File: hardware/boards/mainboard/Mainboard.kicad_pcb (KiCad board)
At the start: 2 copper layers, 114.3 x 101.6 mm, 118 parts, among them IC1 LM340?-MP, J1 MOLEX_52892-3033MOLEX_52892-3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, J2 JST---S4B-PH-SM4-TB(LF)(SN)_J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, U1 CS42448, U2 PCA9536

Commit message: mainboard v1.7
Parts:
- removed J1: MOLEX_52892-3033MOLEX_52892-3033_0_0, Mainboard:MOLEX_52892-3033_0
- removed J2: JST---S4B-PH-SM4-TB(LF)(SN)_JST_S4B-PH-SM4-TB_LF_SNJST_S4B-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, knobs:JST---S4B-PH-SM4-TB(LF)(SN)_JST_S4B-PH-SM4-TB_LF_SN_0
- added U3: Breakoutboard, topbreakout:Breakoutboard, B.Cu at (17.8, 71.1)
- U$1: value TEENSY_4.0_WITH_SMD_HEADER_PINS -> TEENSY_4.0_WITH_SMD_HEADER_PINS_2; footprint Mainboard:TEENSY_4.0_WITH_SMD_HEADER_PINS -> Mainboard:TEENSY_4.0_WITH_SMD_HEADER_PINS_2
- moved JUSB_B1 76.9 mm to (26.0, 68.6)
- moved R1 14.4 mm to (45.7, 22.2)
- moved C54 8.64 mm to (24.8, 59.1)
- moved C53 8.64 mm to (24.8, 55.9)
- moved R31 8.64 mm to (24.9, 53.0)
- moved C51 8.13 mm to (31.8, 62.2)
- moved C49 7.18 mm to (24.8, 38.7)
- moved C50 7.18 mm to (24.8, 41.3)
- moved R27 7.18 mm to (24.9, 35.8)
- moved C47 7.17 mm to (31.7, 43.8)
- moved R33 6.99 mm to (64.1, 67.9)
- moved C52 6.75 mm to (31.8, 52.7)
- moved R29 6.75 mm to (31.8, 55.6)
- moved R30 6.75 mm to (31.8, 58.4)
- moved C43 6.35 mm to (31.8, 27.9)
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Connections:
- net /codec/LEFT renamed /codec/Audio-out/LEFT
- net /codec/LEFT_1 renamed /codec/sheet5D8B3355/LEFT
- net /codec/LEFT_2 renamed /codec/sheet5D8BB035/LEFT
- net /codec/LEFT_3 renamed /codec/sheet5D7A5ED6/LEFT
- net /codec/LEFT_OUT renamed /codec/Audio-in/LEFT_OUT
- net /codec/LEFT_OUT_1 renamed /codec/sheet5D7EAAD2/LEFT_OUT
- net /codec/LEFT_OUT_2 renamed /codec/sheet5D7E3893/LEFT_OUT
- net /codec/RIGHT renamed /codec/Audio-out/RIGHT
- net /codec/RIGHT_1 renamed /codec/sheet5D8BB035/RIGHT
- net /codec/RIGHT_2 renamed /codec/sheet5D8B3355/RIGHT
- net /codec/RIGHT_3 renamed /codec/sheet5D7A5ED6/RIGHT
- net /codec/RIGHT_OUT renamed /codec/sheet5D7E3893/RIGHT_OUT
- net /codec/RIGHT_OUT_1 renamed /codec/Audio-in/RIGHT_OUT
- net /codec/RIGHT_OUT_2 renamed /codec/sheet5D7EAAD2/RIGHT_OUT
- U1 pad 24: +3V3 -> 3V3
- U1 pad 4: +3V3 -> 3V3
- U1 pad 6: +3V3 -> 3V3
- U1 pad 8: +3V3 -> 3V3
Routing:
- net VIN: track 167.0 -> 0.00 mm, vias 1 -> 0
- net +3V3: track 165.0 -> 0.00 mm, vias 2 -> 0
- net SDA: track 148.5 -> 0.00 mm, vias 2 -> 0
- net SCL: track 143.3 -> 0.00 mm, vias 2 -> 0
- net /codec/AVIN: track 96.7 -> 0.00 mm
- net AVSS: track 94.2 -> 0.00 mm, vias 1 -> 0
- net AVDD: track 93.3 -> 0.00 mm, vias 1 -> 0
- net BCLK: track 92.2 -> 0.00 mm, vias 2 -> 0
- net LRCLK: track 87.0 -> 0.00 mm, vias 3 -> 0
- net MCLK: track 83.8 -> 0.00 mm, vias 2 -> 0
- net GND: track 69.6 -> 0.00 mm, vias 89 -> 0
- net DAC_DATA: track 65.3 -> 0.00 mm, vias 1 -> 0
- net ADC_DATA: track 64.1 -> 0.00 mm, vias 1 -> 0
- net /codec/sheet5D8BB035/RIGHT: track 53.5 -> 0.00 mm
- net GATE_1: track 49.1 -> 0.00 mm, vias 1 -> 0
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- removed copper zone on B.Cu, net /codec/AGND
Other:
- board size 114.3 x 101.6 mm -> 118.1 x 101.6 mm

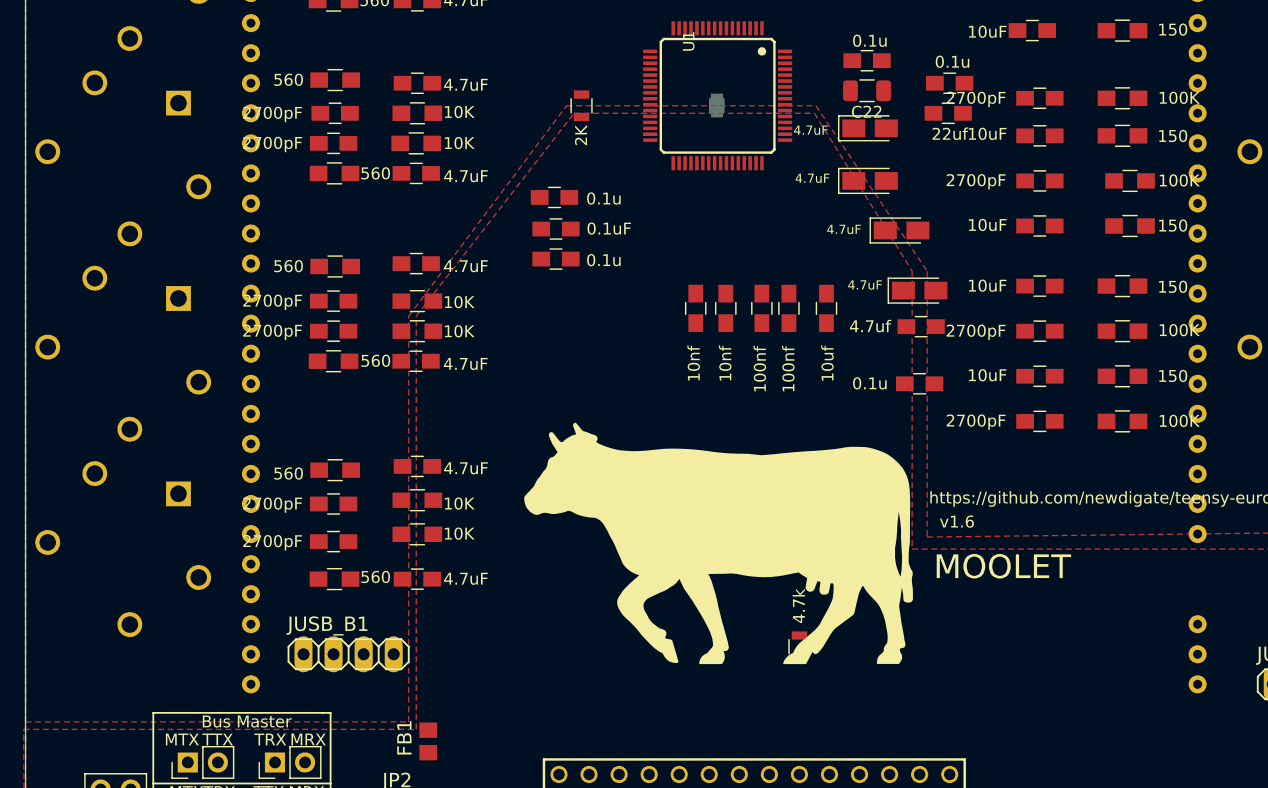
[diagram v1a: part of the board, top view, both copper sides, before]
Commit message: mainboard v1.7 minor changes
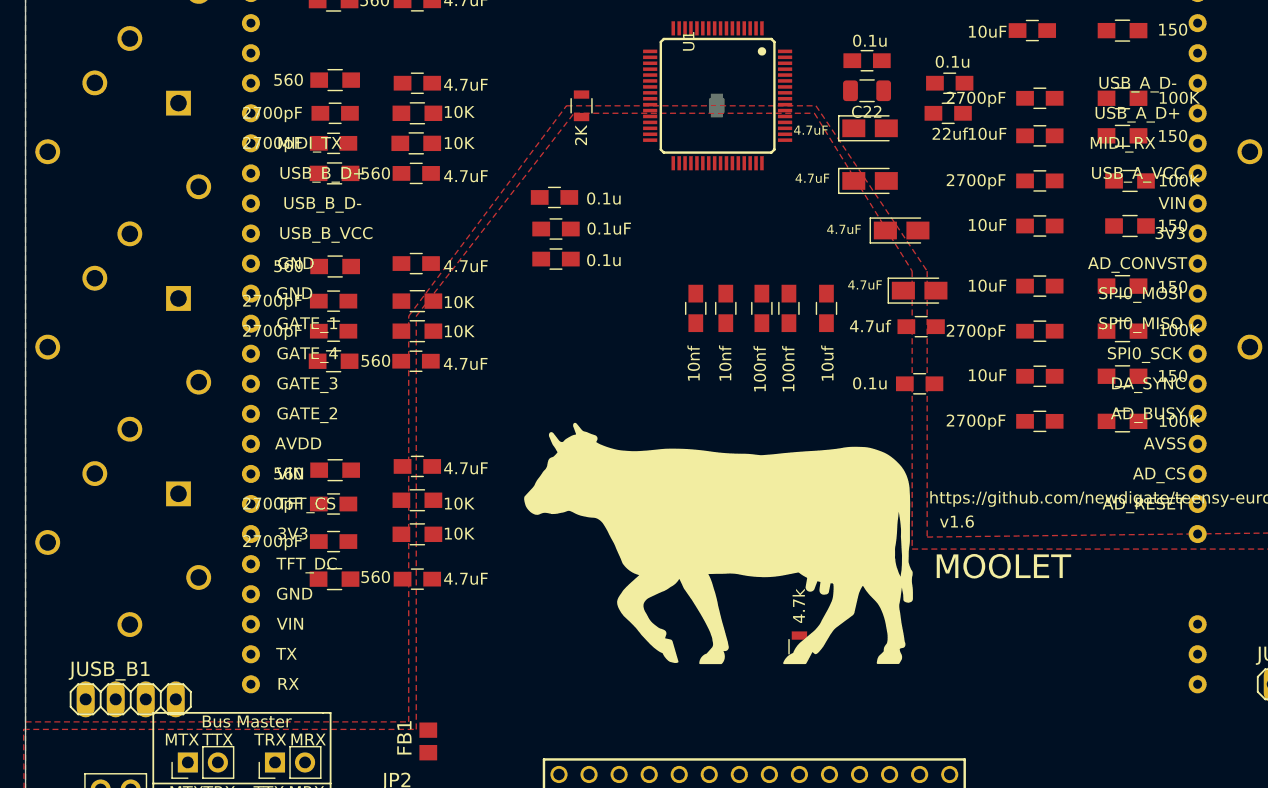
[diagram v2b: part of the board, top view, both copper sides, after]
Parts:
- moved JUSB_B1 18.8 mm to (7.62, 72.4)

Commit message: mainboard v1.7 routed
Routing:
- net VIN: track 0.00 -> 209.8 mm, vias 0 -> 2
- net +3V3: track 0.00 -> 192.5 mm, vias 0 -> 1
- net GATE_2: track 0.00 -> 139.2 mm, vias 0 -> 1
- net SDA: track 0.00 -> 135.5 mm, vias 0 -> 1
- net SCL: track 0.00 -> 134.0 mm, vias 0 -> 1
- net GATE_1: track 0.00 -> 132.0 mm, vias 0 -> 1
- net GATE_3: track 0.00 -> 120.2 mm, vias 0 -> 1
- net GATE_4: track 0.00 -> 118.1 mm, vias 0 -> 1
- net AVSS: track 0.00 -> 118.1 mm
- net SPI0_SCK: track 0.00 -> 93.7 mm
- net MIDI_TX: track 0.00 -> 92.7 mm, vias 0 -> 1
- net BCLK: track 0.00 -> 87.2 mm, vias 0 -> 1
- net LRCLK: track 0.00 -> 87.1 mm, vias 0 -> 1
- net MCLK: track 0.00 -> 84.3 mm, vias 0 -> 1
- net DA_SYNC: track 0.00 -> 81.0 mm
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
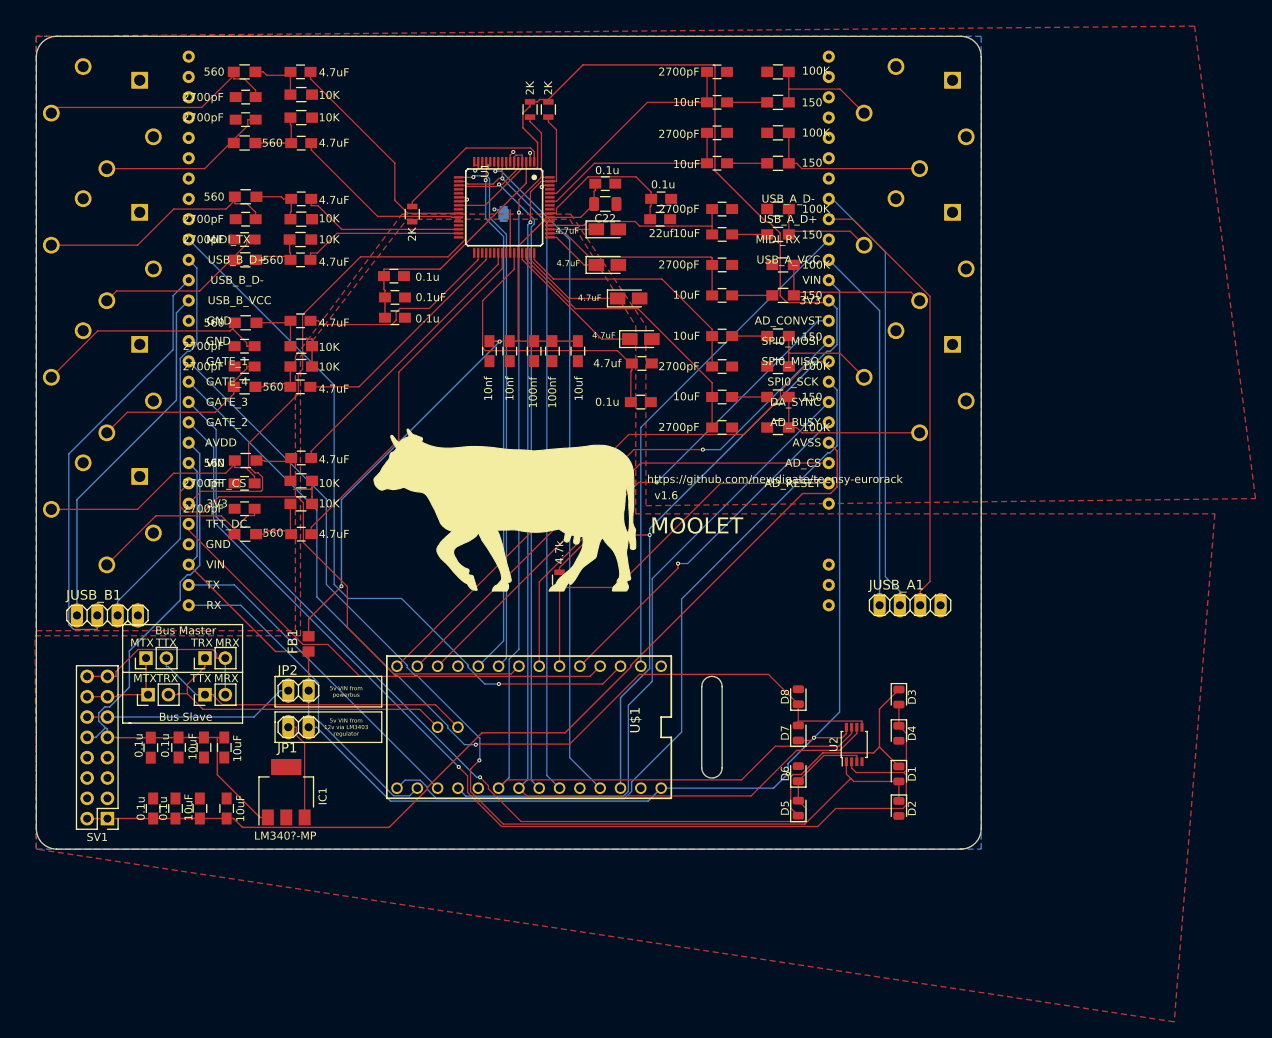
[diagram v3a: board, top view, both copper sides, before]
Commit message: Mainboard DRCed
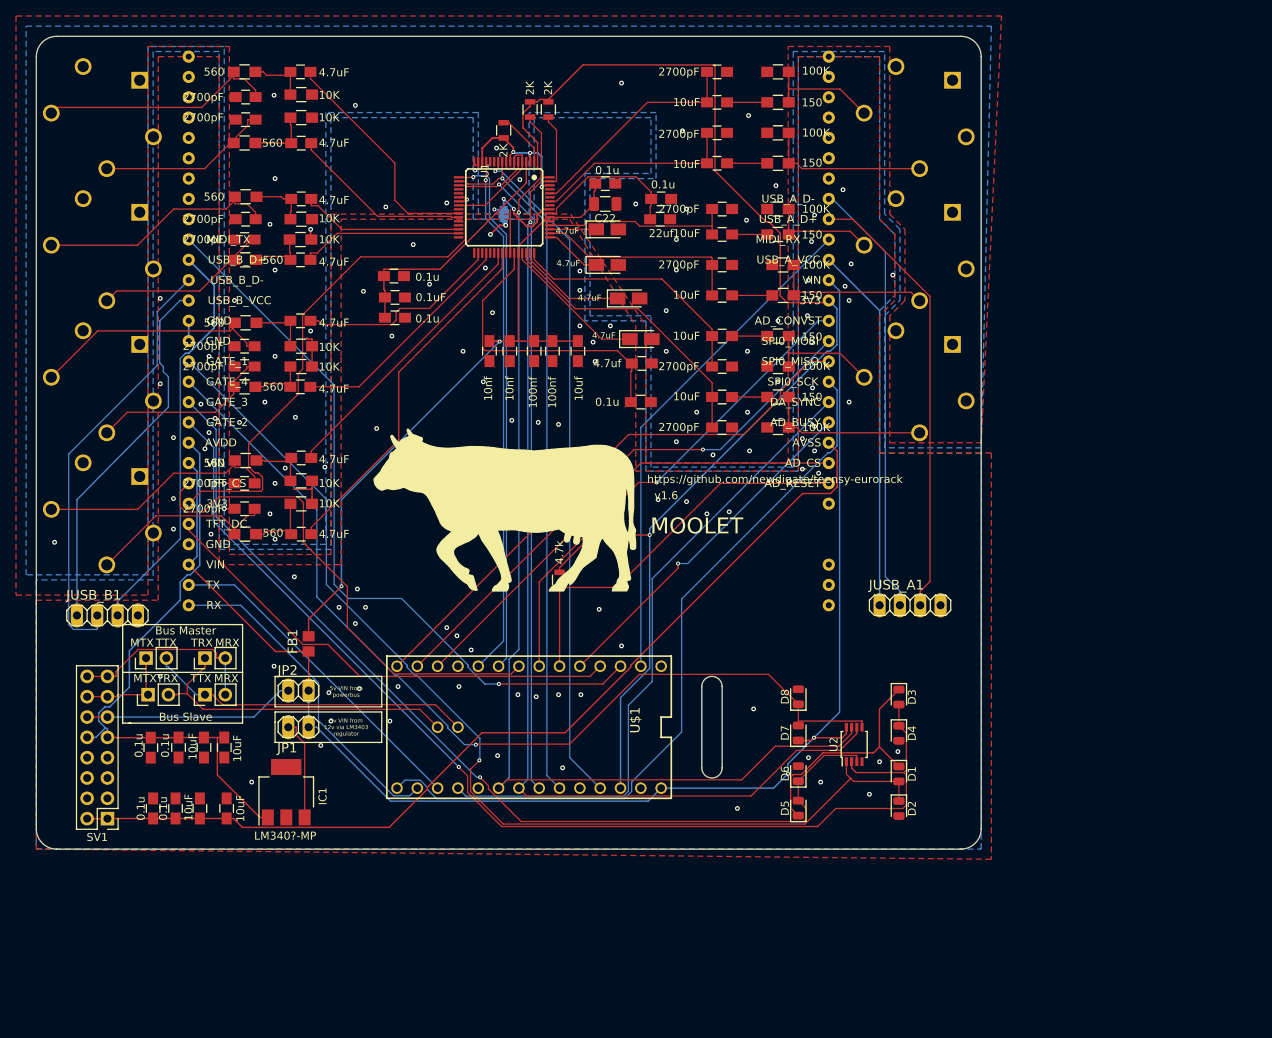
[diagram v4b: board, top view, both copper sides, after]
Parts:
- moved R1 15.5 mm to (57.1, 11.8)
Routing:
- net GND: track 9.60 -> 30.9 mm, vias 5 -> 91
- net /codec/AGND: track 16.0 -> 33.2 mm, vias 1 -> 46
- net Net-(R1-Pad2): track 20.1 -> 6.84 mm
- net /daughter board connectors/USB_B_VCC: track 45.2 -> 47.9 mm
- net /daughter board connectors/USB_B_D+: track 49.1 -> 51.0 mm
- added copper zone on B.Cu, net /codec/AGND

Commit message: mainboard v1.7
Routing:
- net /codec/AGND: track 33.2 -> 72.6 mm, vias 46 -> 48
- net GND: track 30.9 -> 35.7 mm

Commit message: mainboard v1.7
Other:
- board text added: "v1.7"
- board text removed: "v1.6"

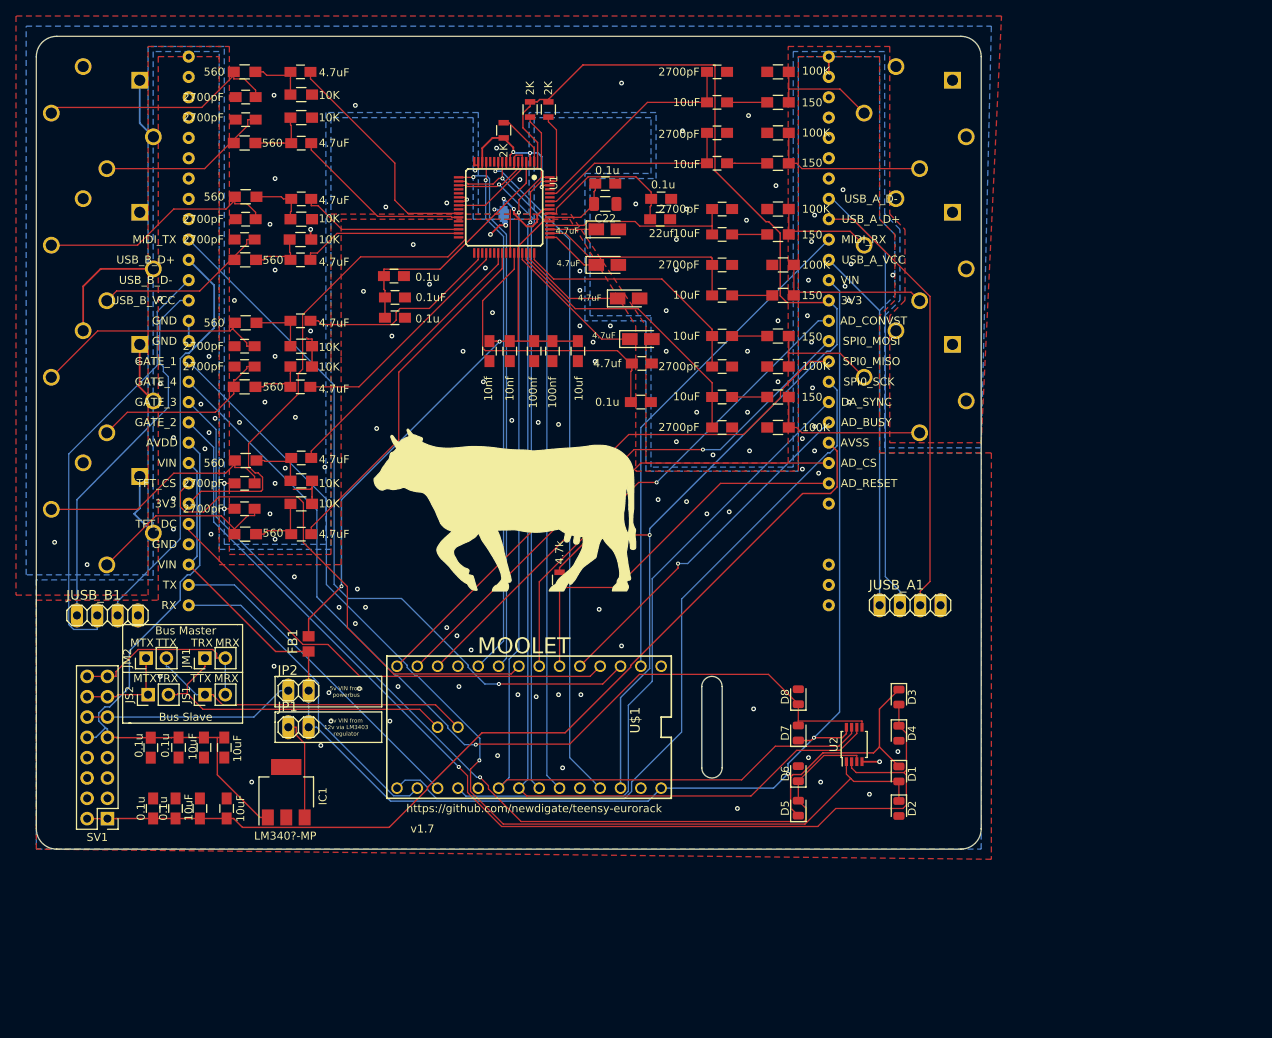
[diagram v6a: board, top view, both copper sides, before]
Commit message: silkscreen impr. & changed 100nF to 0.1uF
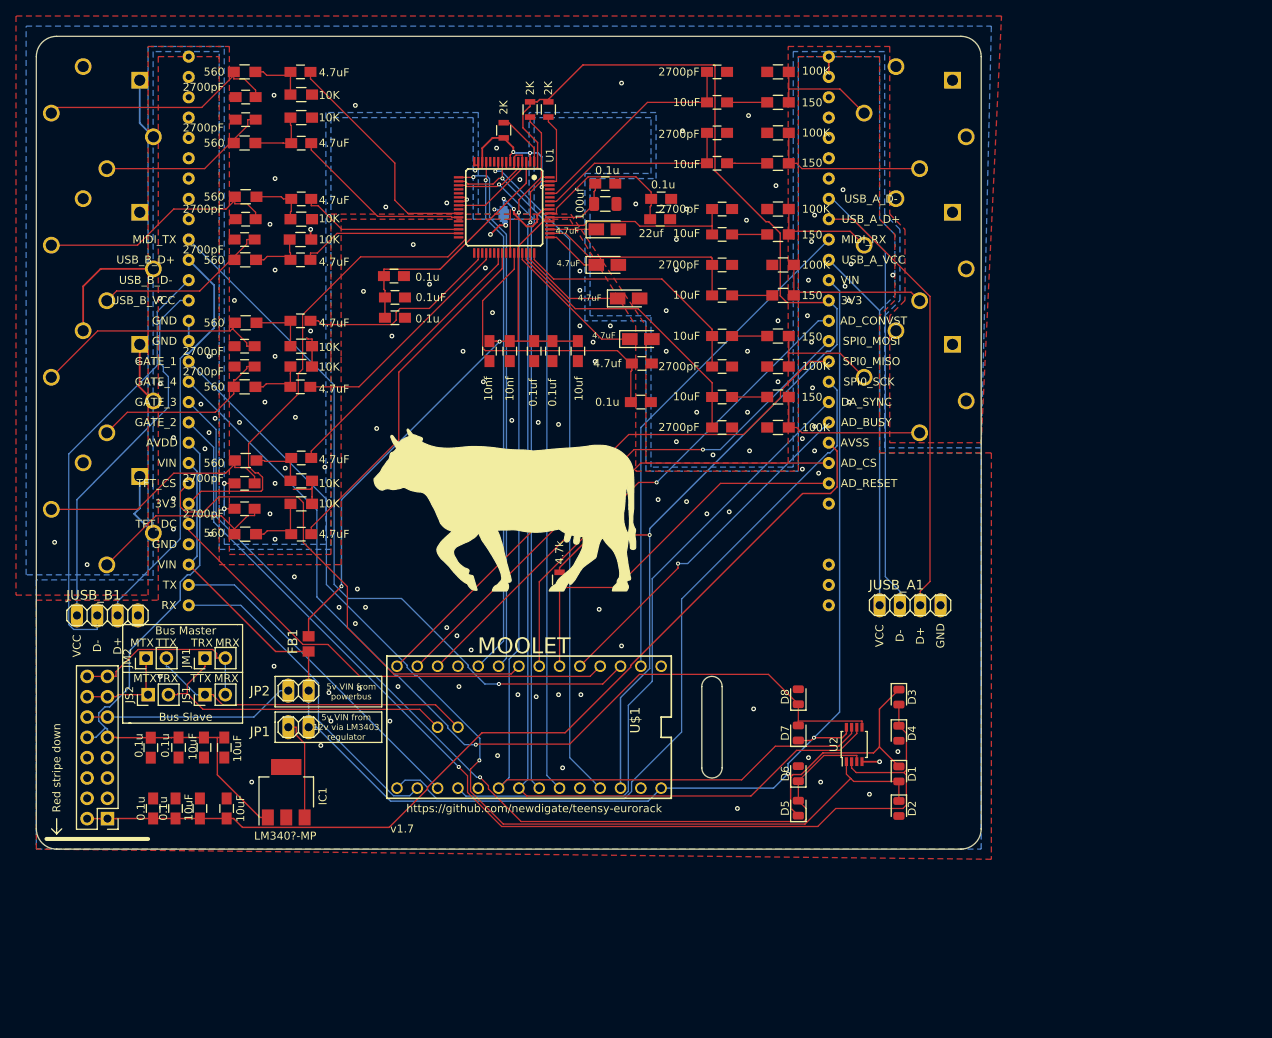
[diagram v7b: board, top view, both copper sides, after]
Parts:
- C17, C18: value 100nf -> 0.1uf
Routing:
- net GND: vias 91 -> 89
- net /daughter board connectors/USB_B_D-: vias 0 -> 1
- net (no net): vias 0 -> 2
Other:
- board text added: "D+"
- board text added: "D-"
- board text added: "GND"
- board text added: "Red stripe down"
- board text added: "VCC"
